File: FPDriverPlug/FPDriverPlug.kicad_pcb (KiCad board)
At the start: 2 copper layers, 21 x 61.6 mm, 4 parts, among them CN1 Conn_02x05_Odd_Even, CN2 Conn_02x16_Counter_Clockwise, U1 FP2800A

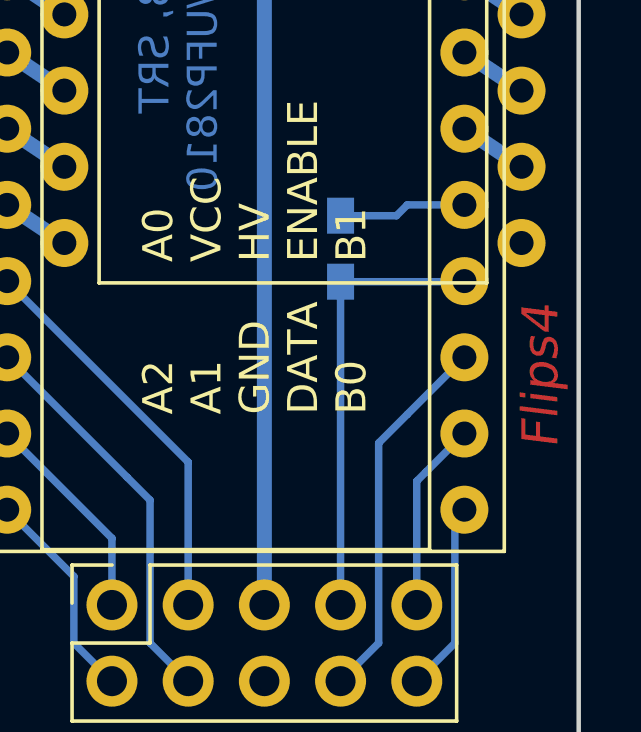
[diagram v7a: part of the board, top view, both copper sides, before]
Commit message: switch resistor to 0805 package
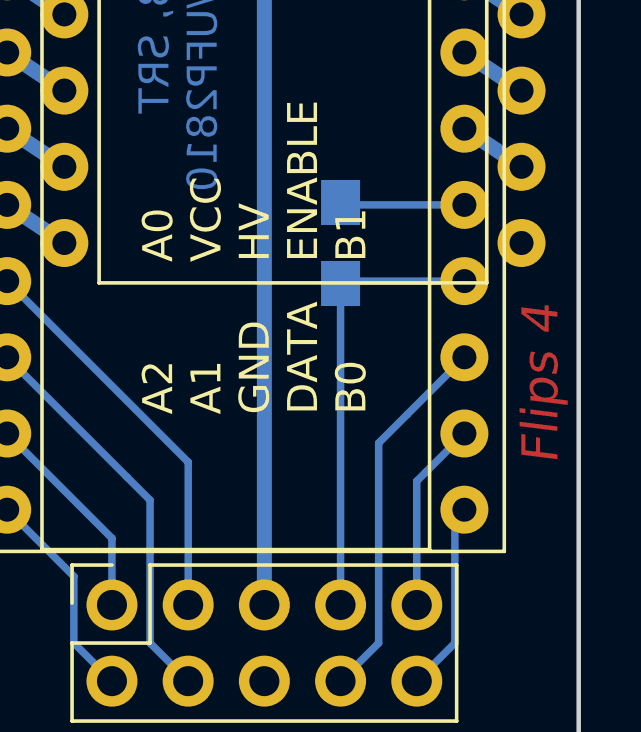
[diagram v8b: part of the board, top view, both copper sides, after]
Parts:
- R1: footprint Resistors_SMD:R_0603_HandSoldering -> Resistors_SMD:R_0805_HandSoldering
- moved R1 0.19 mm to (231.5, 106.0)
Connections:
- CN2 pad 17: (no net) -> Net-(CN2-Pad17)
- CN2 pad 27: (no net) -> Net-(CN2-Pad27)
- CN2 pad 7: (no net) -> Net-(CN2-Pad7)
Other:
- board text removed: "Flips4"
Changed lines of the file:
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@@
     (thickness 1.6)
     (drawings 19)
-    (tracks 60)
+    (tracks 59)
     (zones 0)
     (modules 4)
-    (nets 40)
+    (nets 43)
   )
   (page A4)
@@
   (net 38 /A2)
   (net 39 /A0)
+  (net 40 "Net-(CN2-Pad27)")
+  (net 41 "Net-(CN2-Pad7)")
+  (net 42 "Net-(CN2-Pad17)")
   (net_class Default "Dies ist die voreingestellte Netzklasse."
     (clearance 0.2)
@@
     (add_net /Data)
     (add_net /Enable)
+    (add_net "Net-(CN2-Pad17)")
+    (add_net "Net-(CN2-Pad27)")
+    (add_net "Net-(CN2-Pad7)")
     (add_net VCC)
   )
@@
     (pad 12 thru_hole oval (at 0 27.94) (size 1.6 1.6) (drill 0.8) (layers *.Cu *.Mask)
       (net 9 "Net-(CN2-Pad12)"))
-    (pad 27 thru_hole oval (at 15.24 12.7) (size 1.6 1.6) (drill 0.8) (layers *.Cu *.Mask))
+    (pad 27 thru_hole oval (at 15.24 12.7) (size 1.6 1.6) (drill 0.8) (layers *.Cu *.Mask)
+      (net 40 "Net-(CN2-Pad27)"))
     (pad 11 thru_hole oval (at 0 25.4) (size 1.6 1.6) (drill 0.8) (layers *.Cu *.Mask)
       (net 11 "Net-(CN2-Pad11)"))
@@
     (pad 23 thru_hole oval (at 15.24 22.86) (size 1.6 1.6) (drill 0.8) (layers *.Cu *.Mask)
       (net 24 "Net-(CN2-Pad23)"))
-    (pad 7 thru_hole oval (at 0 15.24) (size 1.6 1.6) (drill 0.8) (layers *.Cu *.Mask))
+    (pad 7 thru_hole oval (at 0 15.24) (size 1.6 1.6) (drill 0.8) (layers *.Cu *.Mask)
+      (net 41 "Net-(CN2-Pad7)"))
     (pad 22 thru_hole oval (at 15.24 25.4) (size 1.6 1.6) (drill 0.8) (layers *.Cu *.Mask)
       (net 26 "Net-(CN2-Pad22)"))
@@
     (pad 2 thru_hole oval (at 0 2.54) (size 1.6 1.6) (drill 0.8) (layers *.Cu *.Mask)
       (net 27 "Net-(CN2-Pad2)"))
-    (pad 17 thru_hole oval (at 15.24 38.1) (size 1.6 1.6) (drill 0.8) (layers *.Cu *.Mask))
+    (pad 17 thru_hole oval (at 15.24 38.1) (size 1.6 1.6) (drill 0.8) (layers *.Cu *.Mask)
+      (net 42 "Net-(CN2-Pad17)"))
     (pad 1 thru_hole circle (at 0 0) (size 1.6 1.6) (drill 0.8) (layers *.Cu *.Mask)
       (net 29 "Net-(CN2-Pad1)"))
@@
     )
   )
-  (module Resistors_SMD:R_0603_HandSoldering (layer B.Cu)
-    (at 231.4575 106.2355 90)
-    (descr "Resistor SMD 0603, hand soldering")
-    (tags "resistor 0603")
+  (module Resistors_SMD:R_0805_HandSoldering (layer B.Cu)
+    (at 231.4575 106.045 90)
+    (descr "Resistor SMD 0805, hand soldering")
+    (tags "resistor 0805")
     (attr smd)
-    (fp_text reference R1 (at 0 1.5875 90) (layer B.SilkS)
+    (fp_text reference R1 (at 0 1.7 90) (layer B.SilkS)
       (effects (font (size 1 1) (thickness 0.15)) (justify mirror))
     )
-    (fp_text value 10K/OPT (at 0 -1.55 90) (layer B.SilkS)
+    (fp_text value 10K/OPT (at 0 -1.75 90) (layer B.Fab)
       (effects (font (size 1 1) (thickness 0.15)) (justify mirror))
     )
-    (fp_line (start 1.95 -0.7) (end -1.96 -0.7) (layer B.CrtYd) (width 0.05))
-    (fp_line (start 1.95 -0.7) (end 1.95 0.7) (layer B.CrtYd) (width 0.05))
-    (fp_line (start -1.96 0.7) (end -1.96 -0.7) (layer B.CrtYd) (width 0.05))
-    (fp_line (start -1.96 0.7) (end 1.95 0.7) (layer B.CrtYd) (width 0.05))
-    (fp_line (start -0.5 0.68) (end 0.5 0.68) (layer B.SilkS) (width 0.12))
-    (fp_line (start 0.5 -0.68) (end -0.5 -0.68) (layer B.SilkS) (width 0.12))
-    (fp_line (start -0.8 0.4) (end 0.8 0.4) (layer B.Fab) (width 0.1))
-    (fp_line (start 0.8 0.4) (end 0.8 -0.4) (layer B.Fab) (width 0.1))
-    (fp_line (start 0.8 -0.4) (end -0.8 -0.4) (layer B.Fab) (width 0.1))
-    (fp_line (start -0.8 -0.4) (end -0.8 0.4) (layer B.Fab) (width 0.1))
-    (fp_text user %R (at -5.165717 -2.514999 90) (layer B.Fab)
-      (effects (font (size 0.4 0.4) (thickness 0.075)) (justify mirror))
-    )
-    (pad 2 smd rect (at 1.1 0 90) (size 1.2 0.9) (layers B.Cu B.Paste B.Mask)
+    (fp_line (start 2.35 -0.9) (end -2.35 -0.9) (layer B.CrtYd) (width 0.05))
+    (fp_line (start 2.35 -0.9) (end 2.35 0.9) (layer B.CrtYd) (width 0.05))
+    (fp_line (start -2.35 0.9) (end -2.35 -0.9) (layer B.CrtYd) (width 0.05))
+    (fp_line (start -2.35 0.9) (end 2.35 0.9) (layer B.CrtYd) (width 0.05))
+    (fp_line (start -0.6 0.88) (end 0.6 0.88) (layer B.SilkS) (width 0.12))
+    (fp_line (start 0.6 -0.88) (end -0.6 -0.88) (layer B.SilkS) (width 0.12))
+    (fp_line (start -1 0.62) (end 1 0.62) (layer B.Fab) (width 0.1))
+    (fp_line (start 1 0.62) (end 1 -0.62) (layer B.Fab) (width 0.1))
+    (fp_line (start 1 -0.62) (end -1 -0.62) (layer B.Fab) (width 0.1))
+    (fp_line (start -1 -0.62) (end -1 0.62) (layer B.Fab) (width 0.1))
+    (fp_text user %R (at 0 0 90) (layer B.Fab)
+      (effects (font (size 0.5 0.5) (thickness 0.075)) (justify mirror))
+    )
+    (pad 2 smd rect (at 1.35 0 90) (size 1.5 1.3) (layers B.Cu B.Paste B.Mask)
       (net 30 GND))
-    (pad 1 smd rect (at -1.1 0 90) (size 1.2 0.9) (layers B.Cu B.Paste B.Mask)
+    (pad 1 smd rect (at -1.35 0 90) (size 1.5 1.3) (layers B.Cu B.Paste B.Mask)
       (net 36 /Enable))
-    (model ${KISYS3DMOD}/Resistors_SMD.3dshapes/R_0603.wrl
+    (model ${KISYS3DMOD}/Resistors_SMD.3dshapes/R_0805.wrl
       (at (xyz 0 0 0))
       (scale (xyz 1 1 1))
@@
     )
   )
-  (gr_text Flips4 (at 238.125 108.077 90) (layer F.Cu)
-    (effects (font (size 1.2 1.2) (thickness 0.24) italic) (justify right))
+  (gr_text "Flips 4" (at 238.125 108.077 90) (layer F.Cu)
+    (effects (font (size 1.2 1.2) (thickness 0.3) italic) (justify right))
   )
   (gr_line (start 218.44 64.77) (end 218.44 126.365) (angle 90) (layer Edge.Cuts) (width 0.15))
@@
   (segment (start 235.585 94.615) (end 237.49 95.885) (width 0.5) (layer B.Cu) (net 28) (status C00000))
   (segment (start 220.345 66.675) (end 222.25 67.945) (width 0.5) (layer B.Cu) (net 29) (status C00000))
-  (segment (start 231.4575 105.1355) (end 233.3195 105.1355) (width 0.25) (layer B.Cu) (net 30) (status 400000))
-  (segment (start 233.3195 105.1355) (end 233.68 104.775) (width 0.25) (layer B.Cu) (net 30))
-  (segment (start 233.68 104.775) (end 235.585 104.775) (width 0.25) (layer B.Cu) (net 30) (status 800000))
+  (segment (start 231.5375 104.775) (end 231.4575 104.695) (width 0.5) (layer B.Cu) (net 30))
+  (segment (start 235.585 104.775) (end 231.5375 104.775) (width 0.25) (layer B.Cu) (net 30))
   (segment (start 220.345 107.315) (end 226.3775 113.3475) (width 0.25) (layer B.Cu) (net 31) (status 400000))
   (segment (start 226.3775 113.3475) (end 226.3775 118.11) (width 0.25) (layer B.Cu) (net 31) (status 800000))
@@
   (segment (start 232.7275 119.38) (end 231.4575 120.65) (width 0.25) (layer B.Cu) (net 35) (status 800000))
   (segment (start 232.7275 112.7125) (end 233.68 111.76) (width 0.25) (layer B.Cu) (net 35))
-  (segment (start 231.4575 107.3355) (end 235.5645 107.3355) (width 0.25) (layer B.Cu) (net 36) (status C00000))
-  (segment (start 235.5645 107.3355) (end 235.585 107.315) (width 0.25) (layer B.Cu) (net 36) (status C00000))
   (segment (start 231.4575 118.11) (end 231.4575 107.3355) (width 0.25) (layer B.Cu) (net 36) (status C00000))
+  (segment (start 231.5375 107.315) (end 231.4575 107.395) (width 0.25) (layer B.Cu) (net 36))
+  (segment (start 235.585 107.315) (end 231.5375 107.315) (width 0.25) (layer B.Cu) (net 36))
   (segment (start 220.345 109.855) (end 224.3455 113.8555) (width 0.25) (layer B.Cu) (net 37) (status 400000))
   (segment (start 225.1075 119.38) (end 225.1075 114.6175) (width 0.25) (layer B.Cu) (net 37))
